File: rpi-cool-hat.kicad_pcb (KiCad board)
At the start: 2 copper layers, 19.3 x 51.1 mm, 3 parts, among them J1 FAN, J2 HAT, J3 RPi

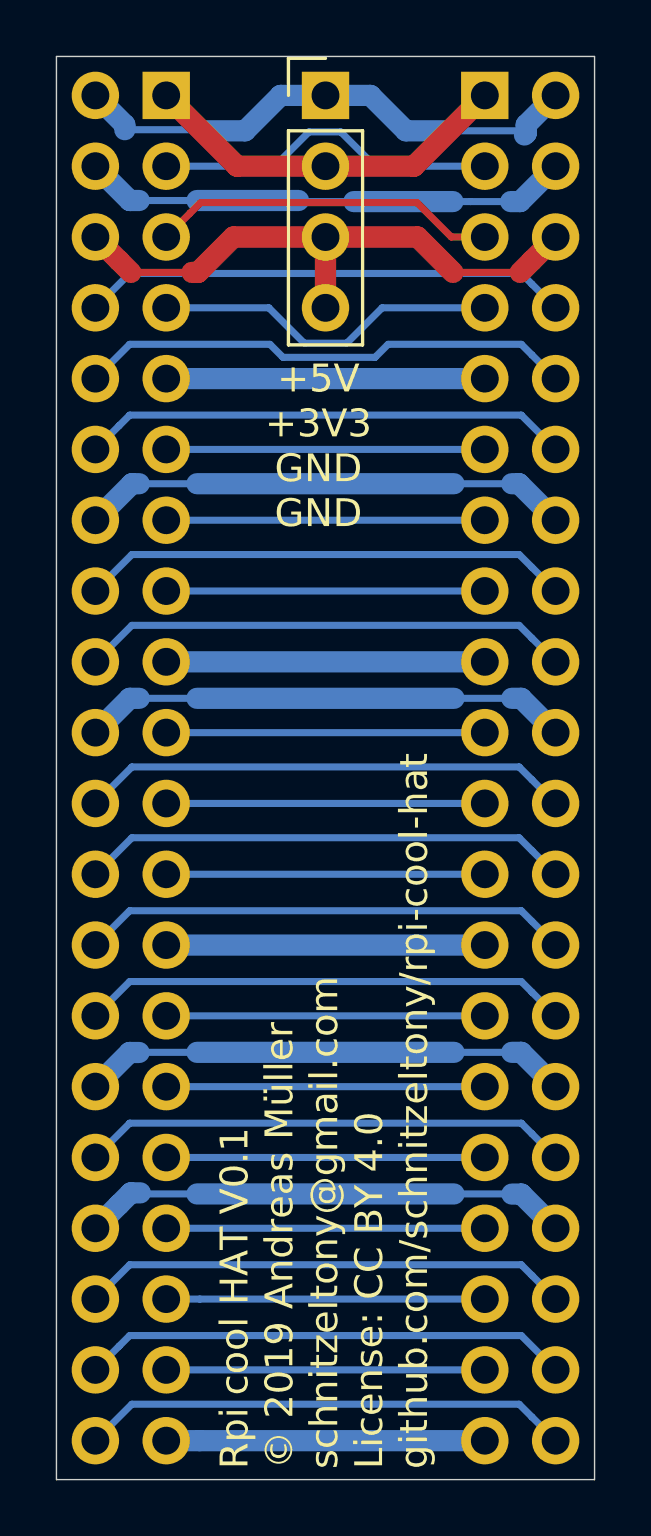
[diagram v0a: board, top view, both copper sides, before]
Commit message: PCB: rework
* Got puzzled with let and right. That caused fan connector pins connected at
  wrong pins.
* Used 50mils for routing which caused cleaner layout
* Reduced PCB size

Signed-off-by: Andreas Müller <schnitzeltony@gmail.com>
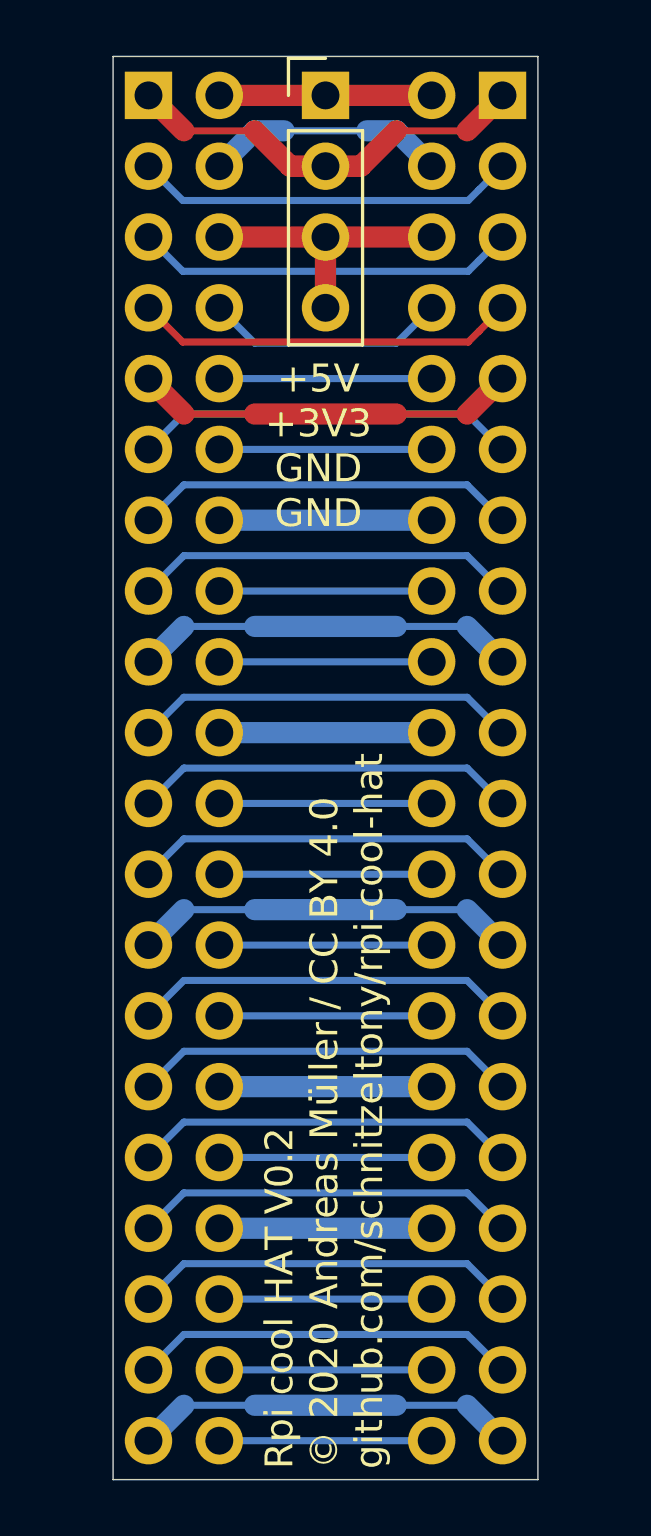
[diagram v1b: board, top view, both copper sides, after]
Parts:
- moved J2 12.1 mm to (146.1, 66.0)
- moved J3 12.1 mm to (133.3, 66.0)
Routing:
- net +5V: track 18.6 -> 7.62 mm
- net GND: track 20.9 -> 10.2 mm
- net Net-(J2-Pad10): track 17.9 -> 7.62 mm
- net Net-(J2-Pad20): track 17.9 -> 7.62 mm
- net Net-(J2-Pad30): track 17.9 -> 7.62 mm
- net Net-(J2-Pad40): track 17.6 -> 7.62 mm
- net Net-(J2-Pad24): track 17.6 -> 7.62 mm
- net Net-(J2-Pad22): track 17.6 -> 7.62 mm
- net Net-(J2-Pad18): track 17.6 -> 7.62 mm
- net Net-(J2-Pad16): track 17.6 -> 7.62 mm
- net Net-(J2-Pad14): track 17.6 -> 7.62 mm
- net Net-(J2-Pad34): track 17.6 -> 7.62 mm
- net Net-(J2-Pad38): track 17.5 -> 7.62 mm
- net Net-(J2-Pad32): track 17.5 -> 7.62 mm
- net Net-(J2-Pad28): track 17.5 -> 7.62 mm
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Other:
- board size 19.3 x 51.1 mm -> 15.2 x 51.1 mm
- board text added: "Rpi cool HAT V0.2 © 2020 Andreas Müller / CC BY 4.0 github.com/schnitzeltony/rpi-cool-hat"
- board text removed: "Rpi cool HAT V0.1 © 2019 Andreas Müller schnitzeltony@gmail.com License: CC BY 4.0 github.com/schnitzeltony/rpi-cool-hat"
